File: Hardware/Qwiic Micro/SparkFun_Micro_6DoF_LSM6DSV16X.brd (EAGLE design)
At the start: 19.1 x 7.6 mm, 41 parts, among them J1 Qwiic Right Angle, U2 LSM6DSV16X

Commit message: Adds silk of the part name
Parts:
- added U$6: (no value), bot:LSM6DSV16X31
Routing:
- net GND: track 6.01 -> 8.45 mm
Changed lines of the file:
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@@
 <setting verticaltext="up"/>
 </settings>
-<grid distance="0.05" unitdist="inch" unit="inch" style="dots" multiple="1" display="yes" altdistance="0.001" altunitdist="inch" altunit="inch"/>
+<grid distance="0.05" unitdist="inch" unit="inch" style="dots" multiple="1" display="yes" altdistance="0.005" altunitdist="inch" altunit="inch"/>
 <layers>
 <layer number="1" name="Top" color="4" fill="1" visible="yes" active="yes"/>
@@
 <attribute name="VALUE" x="9.525" y="5.556" size="0.6096" layer="27" font="vector" ratio="20" rot="R180" align="center"/>
 </element>
+<element name="U$6" library="bot" package="LSM6DSV16X31" value="" x="6.223" y="3.81" smashed="yes" rot="R90"/>
 </elements>
 <signals>
@@
 <wire x1="9.025" y1="5.20936875" x2="9.13693125" y2="5.3213" width="0.2794" layer="1"/>
 <via x="8.7122" y="6.223" extent="1-16" drill="0.3"/>
+<wire x1="9.525" y1="4.81" x2="9.525" y2="3.81" width="0.254" layer="1"/>
+<wire x1="9.525" y1="3.81" x2="9.398" y2="3.937" width="0.254" layer="1"/>
+<wire x1="9.398" y1="3.937" x2="9.017" y2="3.937" width="0.254" layer="1"/>
+<wire x1="9.017" y1="3.937" x2="9.017" y2="4.802" width="0.254" layer="1"/>
+<wire x1="9.017" y1="4.802" x2="9.025" y2="4.81" width="0.254" layer="1"/>
 </signal>
 <signal name="SCL">

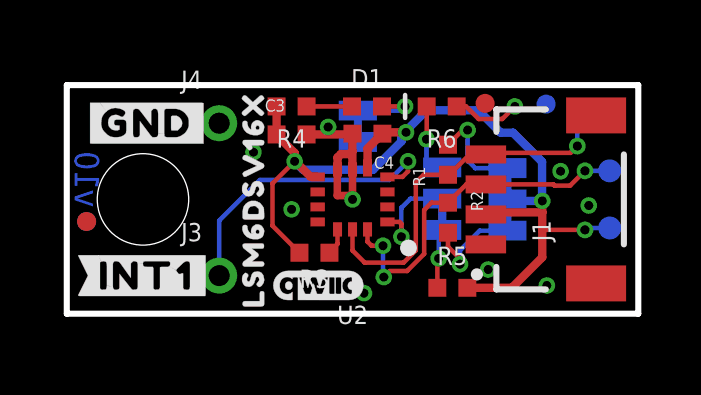
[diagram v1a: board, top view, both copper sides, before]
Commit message: Updates measures, fixes various DRC issues in micro
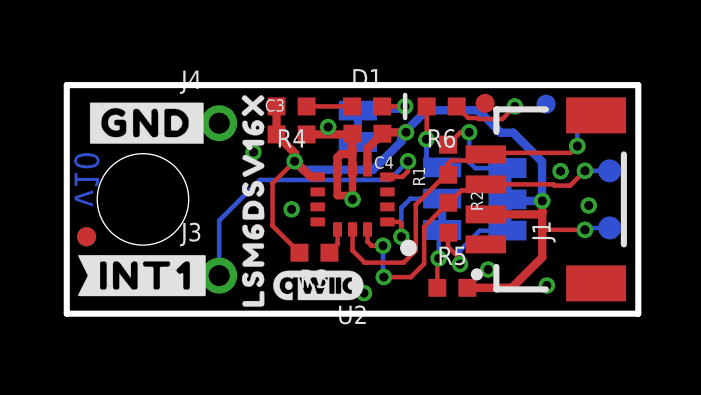
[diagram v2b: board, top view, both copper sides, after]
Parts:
- moved U$29 7.83 mm to (10.4, 3.43)
- moved LOGO2 1.05 mm to (16.7, 1.38)
- moved U$12 0.76 mm to (16.4, 4.57)
- moved FD2 0.51 mm to (0.66, 2.57)
- moved FID2 0.51 mm to (0.66, 2.57)

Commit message: Updates part with silk outline
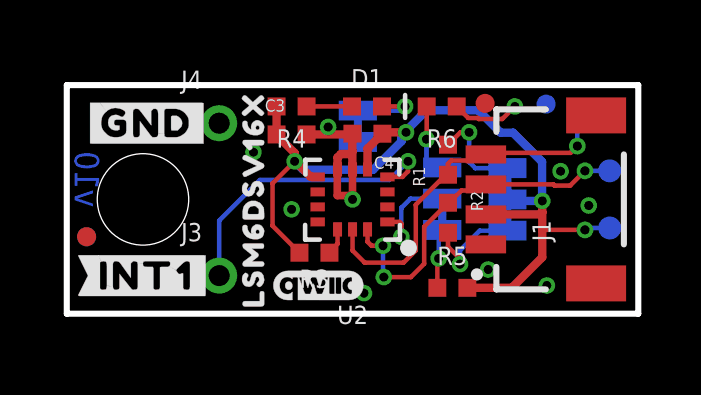
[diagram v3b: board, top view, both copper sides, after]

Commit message: Adds proto gerbers
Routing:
- net GND: track 8.45 -> 10.5 mm
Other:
- board text added: "v01"
- board text removed: "v10"
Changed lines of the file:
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@@
 <layer number="39" name="tKeepout" color="4" fill="11" visible="no" active="yes"/>
 <layer number="40" name="bKeepout" color="1" fill="11" visible="no" active="yes"/>
-<layer number="41" name="tRestrict" color="4" fill="10" visible="no" active="yes"/>
+<layer number="41" name="tRestrict" color="4" fill="10" visible="yes" active="yes"/>
 <layer number="42" name="bRestrict" color="1" fill="10" visible="no" active="yes"/>
 <layer number="43" name="vRestrict" color="2" fill="10" visible="no" active="yes"/>
@@
 <wire x1="0" y1="0" x2="19.05" y2="0" width="0.2032" layer="20"/>
 <wire x1="19.05" y1="0" x2="19.05" y2="7.62" width="0.2032" layer="20"/>
-<text x="0.263525" y="3.546475" size="0.8128" layer="16" font="vector" ratio="22" rot="SMR90">v10</text>
+<text x="0.263525" y="3.546475" size="0.8128" layer="16" font="vector" ratio="22" rot="SMR90">v01</text>
 <rectangle x1="9.1948" y1="4.953" x2="9.2456" y2="5.1816" layer="41"/>
 <dimension x1="2.54" y1="3.81" x2="0" y2="3.81" x3="1.27" y3="12.7" textsize="1.778" layer="47" dtype="horizontal" unit="inch"/>
@@
 <wire x1="14.5161" y1="6.4897" x2="14.8082" y2="6.7818" width="0.1524" layer="1"/>
 <wire x1="13.3802" y1="6.5254" x2="13.69321875" y2="6.5254" width="0.1524" layer="1"/>
+<wire x1="4.5974" y1="0.4064" x2="5.6134" y2="0.4064" width="0.254" layer="16"/>
+<wire x1="4.5974" y1="7.2136" x2="5.6134" y2="7.2136" width="0.254" layer="16"/>
 </signal>
 <signal name="SCL">
@@
 <wire x1="10.75295" y1="4.4577" x2="6.4389" y2="4.4577" width="0.1524" layer="16"/>
 <contactref element="J3" pad="1"/>
-<wire x1="5.08" y1="3.0988" x2="5.08" y2="1.27" width="0.1524" layer="16"/>
-<wire x1="6.4389" y1="4.4577" x2="5.08" y2="3.0988" width="0.1524" layer="16"/>
+<wire x1="5.588" y1="3.6068" x2="5.588" y2="1.778" width="0.1524" layer="16"/>
+<wire x1="5.588" y1="1.778" x2="5.08" y2="1.27" width="0.1524" layer="16"/>
+<wire x1="6.4389" y1="4.4577" x2="5.588" y2="3.6068" width="0.1524" layer="16"/>
 <contactref element="U2" pad="P4"/>
 <wire x1="10.6875" y1="4.56" x2="11.1894" y2="4.56" width="0.1524" layer="1"/>

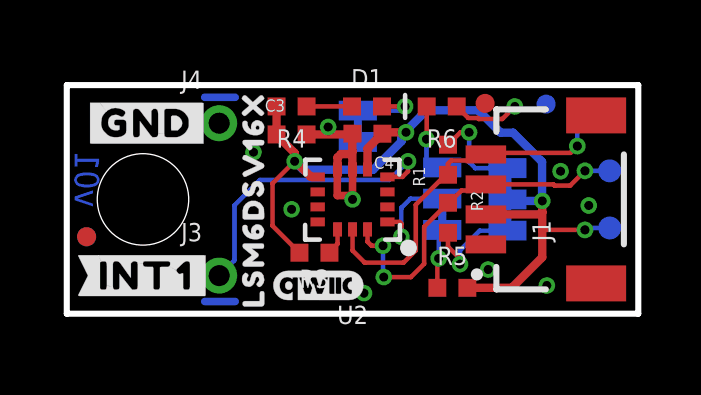
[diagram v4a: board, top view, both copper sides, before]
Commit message: Rolls version to v10 on Micro, increases the size of the pin one indicator for the LED
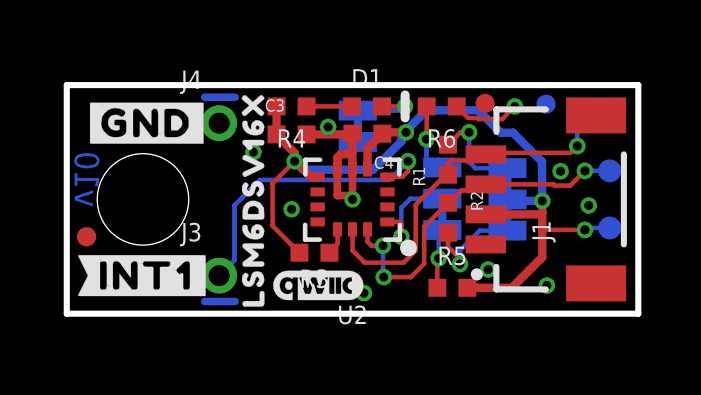
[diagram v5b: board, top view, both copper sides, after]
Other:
- board text added: "v10"
- board text removed: "v01"
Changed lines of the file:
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@@
 <layer number="39" name="tKeepout" color="4" fill="11" visible="no" active="yes"/>
 <layer number="40" name="bKeepout" color="1" fill="11" visible="no" active="yes"/>
-<layer number="41" name="tRestrict" color="4" fill="10" visible="yes" active="yes"/>
+<layer number="41" name="tRestrict" color="4" fill="10" visible="no" active="yes"/>
 <layer number="42" name="bRestrict" color="1" fill="10" visible="no" active="yes"/>
 <layer number="43" name="vRestrict" color="2" fill="10" visible="no" active="yes"/>
@@
 <wire x1="0" y1="0" x2="19.05" y2="0" width="0.2032" layer="20"/>
 <wire x1="19.05" y1="0" x2="19.05" y2="7.62" width="0.2032" layer="20"/>
-<text x="0.263525" y="3.546475" size="0.8128" layer="16" font="vector" ratio="22" rot="SMR90">v01</text>
+<text x="0.263525" y="3.546475" size="0.8128" layer="16" font="vector" ratio="22" rot="SMR90">v10</text>
 <rectangle x1="9.1948" y1="4.953" x2="9.2456" y2="5.1816" layer="41"/>
 <dimension x1="2.54" y1="3.81" x2="0" y2="3.81" x3="1.27" y3="12.7" textsize="1.778" layer="47" dtype="horizontal" unit="inch"/>
@@
 <dimension x1="13.97" y1="3.81" x2="13.97" y2="7.62" x3="22.86" y3="5.715" textsize="1.778" textratio="15" layer="47" unit="inch"/>
 <text x="-1.27" y="-10.16" size="1.778" layer="47" font="vector">Units in Inches</text>
+<wire x1="11.2776" y1="7.2898" x2="11.2776" y2="6.5278" width="0.3048" layer="21"/>
 </plain>
 <attributes>

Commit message: Grounds SCx and SDx on  micro since they are not used
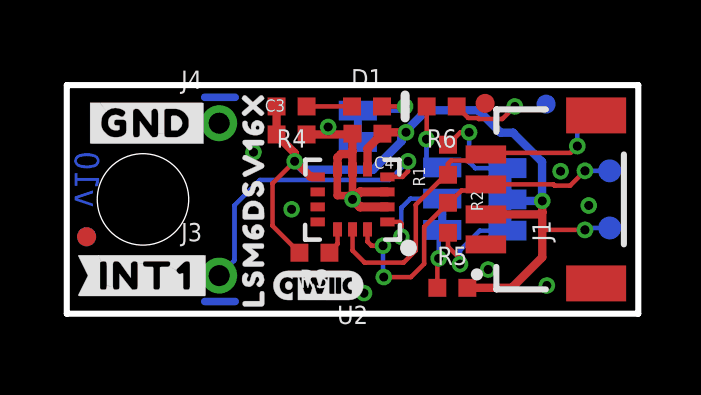
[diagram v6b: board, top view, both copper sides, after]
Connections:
- net GND: now also U2.P2, U2.P3
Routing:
- net GND: track 10.5 -> 13.0 mm
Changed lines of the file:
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@@
 <layer number="39" name="tKeepout" color="4" fill="11" visible="no" active="yes"/>
 <layer number="40" name="bKeepout" color="1" fill="11" visible="no" active="yes"/>
-<layer number="41" name="tRestrict" color="4" fill="10" visible="no" active="yes"/>
+<layer number="41" name="tRestrict" color="4" fill="10" visible="yes" active="yes"/>
 <layer number="42" name="bRestrict" color="1" fill="10" visible="no" active="yes"/>
 <layer number="43" name="vRestrict" color="2" fill="10" visible="no" active="yes"/>
@@
 <wire x1="19.05" y1="0" x2="19.05" y2="7.62" width="0.2032" layer="20"/>
 <text x="0.263525" y="3.546475" size="0.8128" layer="16" font="vector" ratio="22" rot="SMR90">v10</text>
-<rectangle x1="9.1948" y1="4.953" x2="9.2456" y2="5.1816" layer="41"/>
+<rectangle x1="9.2202" y1="4.9276" x2="9.271" y2="5.1562" layer="41"/>
 <dimension x1="2.54" y1="3.81" x2="0" y2="3.81" x3="1.27" y3="12.7" textsize="1.778" layer="47" dtype="horizontal" unit="inch"/>
 <wire x1="5.207" y1="3.171825" x2="7.112" y2="3.171825" width="0.254" layer="22"/>
@@
 <text x="-1.27" y="-10.16" size="1.778" layer="47" font="vector">Units in Inches</text>
 <wire x1="11.2776" y1="7.2898" x2="11.2776" y2="6.5278" width="0.3048" layer="21"/>
+<rectangle x1="10.6553" y1="3.6957" x2="10.7061" y2="3.9243" layer="41" rot="R90"/>
 </plain>
 <attributes>
@@
 <contactref element="U2" pad="P6"/>
 <contactref element="U2" pad="P7"/>
-<wire x1="14.8082" y1="6.7818" x2="14.9352" y2="6.9088" width="0.1524" layer="1"/>
 <wire x1="9.4535" y1="5.97535" x2="9.4742" y2="5.95465" width="0.2794" layer="1"/>
 <wire x1="7.993" y1="5.97535" x2="9.4535" y2="5.97535" width="0.2794" layer="1"/>
@@
 <wire x1="13.69321875" y1="6.5254" x2="13.72891875" y2="6.4897" width="0.1524" layer="1"/>
 <wire x1="13.72891875" y1="6.4897" x2="14.5161" y2="6.4897" width="0.1524" layer="1"/>
-<wire x1="14.5161" y1="6.4897" x2="14.8082" y2="6.7818" width="0.1524" layer="1"/>
+<wire x1="14.5161" y1="6.4897" x2="14.9352" y2="6.9088" width="0.1524" layer="1"/>
 <wire x1="13.3802" y1="6.5254" x2="13.69321875" y2="6.5254" width="0.1524" layer="1"/>
 <wire x1="4.5974" y1="0.4064" x2="5.6134" y2="0.4064" width="0.254" layer="16"/>
 <wire x1="4.5974" y1="7.2136" x2="5.6134" y2="7.2136" width="0.254" layer="16"/>
+<contactref element="U2" pad="P2"/>
+<contactref element="U2" pad="P3"/>
+<wire x1="10.6875" y1="4.06" x2="9.775" y2="4.06" width="0.3048" layer="1"/>
+<wire x1="9.775" y1="4.06" x2="9.525" y2="3.81" width="0.3048" layer="1"/>
+<wire x1="10.6875" y1="3.56" x2="9.775" y2="3.56" width="0.3048" layer="1"/>
+<wire x1="9.775" y1="3.56" x2="9.525" y2="3.81" width="0.3048" layer="1"/>
 </signal>
 <signal name="SCL">
